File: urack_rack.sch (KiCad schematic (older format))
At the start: 20 parts, among them J1 Screw_Terminal_01x03, U1 LM1117-5.0, U2 MC7905

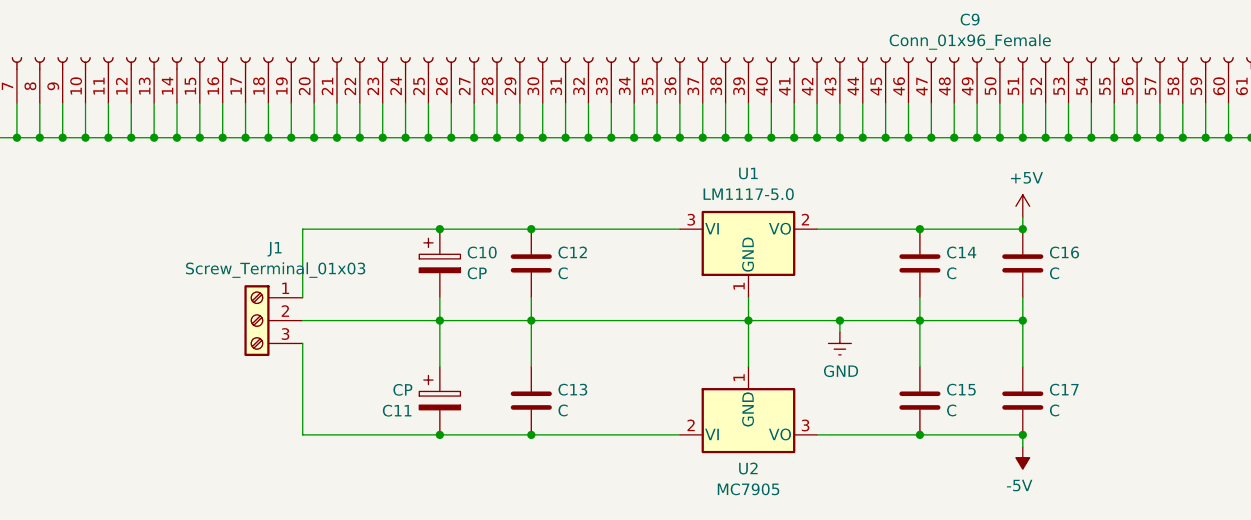
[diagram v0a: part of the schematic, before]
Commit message: Delete LDO. New size connector
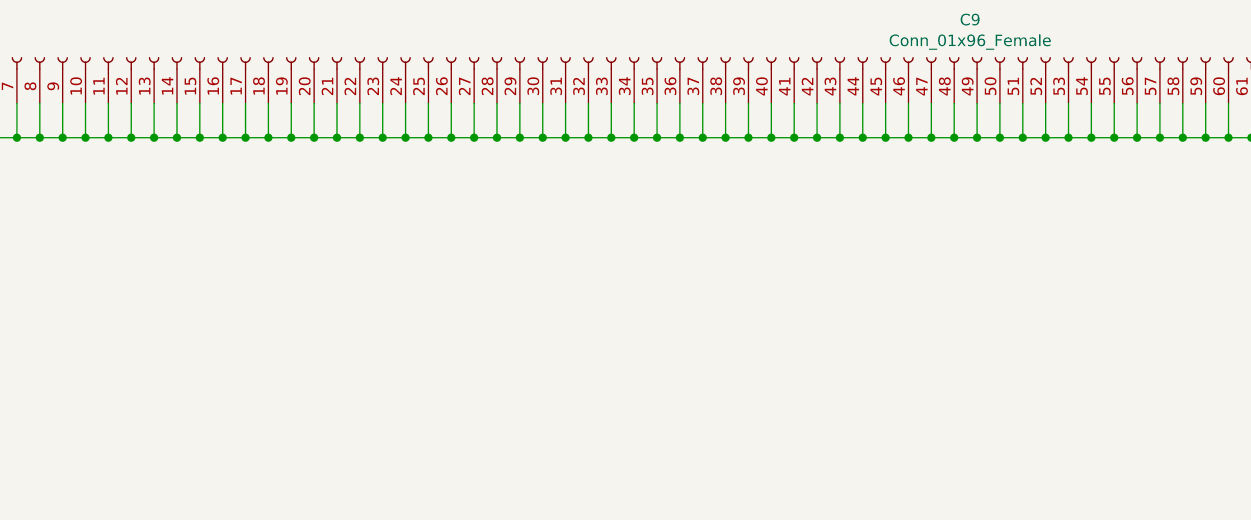
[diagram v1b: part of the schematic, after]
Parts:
- removed C10, C11: CP, Capacitor_SMD:CP_Elec_6.3x7.7, symbol Device:CP
- removed C12, C13, C14, C15, C16, C17: C, Capacitor_SMD:C_0603_1608Metric_Pad1.05x0.95mm_HandSolder, symbol Device:C
- removed J1: Screw_Terminal_01x03, TerminalBlock_Phoenix:TerminalBlock_Phoenix_PT-1,5-3-3.5-H_1x03_P3.50mm_Horizontal, symbol Connector:Screw_Terminal_01x03
- removed U1: LM1117-5.0, Package_TO_SOT_SMD:TO-252-2, symbol Regulator_Linear:LM1117-5.0
- removed U2: MC7905, Package_TO_SOT_SMD:TO-263-3_TabPin2, symbol Regulator_Linear:MC7905
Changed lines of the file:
@@
 Wire Wire Line
 	8050 1800 7950 1800
-$Comp
-L Regulator_Linear:LM1117-5.0 U1
-U 1 1 5FD46628
-P 4550 6450
-F 0 "U1" H 4550 6692 50  0000 C CNN
-F 1 "LM1117-5.0" H 4550 6601 50  0000 C CNN
-F 2 "Package_TO_SOT_SMD:TO-252-2" H 4550 6450 50  0001 C CNN
-F 3 "http://www.ti.com/lit/ds/symlink/lm1117.pdf" H 4550 6450 50  0001 C CNN
-	1    4550 6450
-	1    0    0    -1
-$EndComp
-$Comp
-L Regulator_Linear:MC7905 U2
-U 1 1 5FD495BC
-P 4550 7350
-F 0 "U2" H 4550 7201 50  0000 C CNN
-F 1 "MC7905" H 4550 7110 50  0000 C CNN
-F 2 "Package_TO_SOT_SMD:TO-263-3_TabPin2" H 4550 7150 50  0001 C CIN
-F 3 "http://www.onsemi.com/pub/Collateral/MC7900-D.PDF" H 4550 7350 50  0001 C CNN
-	1    4550 7350
-	1    0    0    -1
-$EndComp
-Wire Wire Line
-	4550 6750 4550 6850
-$Comp
-L uRack:GND #PWR0104
-U 1 1 6073BE97
-P 4950 6900
-F 0 "#PWR0104" H 4950 6650 50  0001 C CNN
-F 1 "GND" H 4955 6727 50  0000 C CNN
-F 2 "" H 4950 6900 50  0001 C CNN
-F 3 "" H 4950 6900 50  0001 C CNN
-	1    4950 6900
-	1    0    0    -1
-$EndComp
-$Comp
-L uRack:+5V #PWR0105
-U 1 1 6073C5B9
-P 5750 6400
-F 0 "#PWR0105" H 5750 6250 50  0001 C CNN
-F 1 "+5V" H 5765 6573 50  0000 C CNN
-F 2 "" H 5750 6400 50  0001 C CNN
-F 3 "" H 5750 6400 50  0001 C CNN
-	1    5750 6400
-	1    0    0    -1
-$EndComp
-$Comp
-L uRack:-5V #PWR0106
-U 1 1 6073FBF9
-P 5750 7400
-F 0 "#PWR0106" H 5750 7500 50  0001 C CNN
-F 1 "-5V" H 5765 7573 50  0000 C CNN
-F 2 "" H 5750 7400 50  0001 C CNN
-F 3 "" H 5750 7400 50  0001 C CNN
-	1    5750 7400
-	-1   0    0    1
-$EndComp
-Wire Wire Line
-	4850 7350 5300 7350
-Wire Wire Line
-	5750 7350 5750 7400
-Wire Wire Line
-	4850 6450 5300 6450
-Wire Wire Line
-	5750 6450 5750 6400
-Wire Wire Line
-	4550 6850 4950 6850
-Wire Wire Line
-	4950 6850 4950 6900
-Connection ~ 4550 6850
-Wire Wire Line
-	4550 6850 4550 7050
-$Comp
-L Device:C C12
-U 1 1 6114C496
-P 3600 6600
-F 0 "C12" H 3715 6646 50  0000 L CNN
-F 1 "C" H 3715 6555 50  0000 L CNN
-F 2 "Capacitor_SMD:C_0603_1608Metric_Pad1.05x0.95mm_HandSolder" H 3638 6450 50  0001 C CNN
-F 3 "~" H 3600 6600 50  0001 C CNN
-	1    3600 6600
-	1    0    0    -1
-$EndComp
-$Comp
-L Device:C C13
-U 1 1 6114E359
-P 3600 7200
-F 0 "C13" H 3715 7246 50  0000 L CNN
-F 1 "C" H 3715 7155 50  0000 L CNN
-F 2 "Capacitor_SMD:C_0603_1608Metric_Pad1.05x0.95mm_HandSolder" H 3638 7050 50  0001 C CNN
-F 3 "~" H 3600 7200 50  0001 C CNN
-	1    3600 7200
-	1    0    0    -1
-$EndComp
-$Comp
-L Device:C C14
-U 1 1 6114F64B
-P 5300 6600
-F 0 "C14" H 5415 6646 50  0000 L CNN
-F 1 "C" H 5415 6555 50  0000 L CNN
-F 2 "Capacitor_SMD:C_0603_1608Metric_Pad1.05x0.95mm_HandSolder" H 5338 6450 50  0001 C CNN
-F 3 "~" H 5300 6600 50  0001 C CNN
-	1    5300 6600
-	1    0    0    -1
-$EndComp
-Connection ~ 5300 6450
-Wire Wire Line
-	5300 6450 5750 6450
-$Comp
-L Device:C C15
-U 1 1 611520D9
-P 5300 7200
-F 0 "C15" H 5415 7246 50  0000 L CNN
-F 1 "C" H 5415 7155 50  0000 L CNN
-F 2 "Capacitor_SMD:C_0603_1608Metric_Pad1.05x0.95mm_HandSolder" H 5338 7050 50  0001 C CNN
-F 3 "~" H 5300 7200 50  0001 C CNN
-	1    5300 7200
-	1    0    0    -1
-$EndComp
-Connection ~ 5300 7350
-Wire Wire Line
-	5300 7350 5750 7350
-$Comp
-L Device:C C16
-U 1 1 61152873
-P 5750 6600
-F 0 "C16" H 5865 6646 50  0000 L CNN
-F 1 "C" H 5865 6555 50  0000 L CNN
-F 2 "Capacitor_SMD:C_0603_1608Metric_Pad1.05x0.95mm_HandSolder" H 5788 6450 50  0001 C CNN
-F 3 "~" H 5750 6600 50  0001 C CNN
-	1    5750 6600
-	1    0    0    -1
-$EndComp
-Connection ~ 5750 6450
-$Comp
-L Device:C C17
-U 1 1 61153349
-P 5750 7200
-F 0 "C17" H 5865 7246 50  0000 L CNN
-F 1 "C" H 5865 7155 50  0000 L CNN
-F 2 "Capacitor_SMD:C_0603_1608Metric_Pad1.05x0.95mm_HandSolder" H 5788 7050 50  0001 C CNN
-F 3 "~" H 5750 7200 50  0001 C CNN
-	1    5750 7200
-	1    0    0    -1
-$EndComp
-Connection ~ 5750 7350
-$Comp
-L Device:CP C10
-U 1 1 61153D94
-P 3200 6600
-F 0 "C10" H 3318 6646 50  0000 L CNN
-F 1 "CP" H 3318 6555 50  0000 L CNN
-F 2 "Capacitor_SMD:CP_Elec_6.3x7.7" H 3238 6450 50  0001 C CNN
-F 3 "~" H 3200 6600 50  0001 C CNN
-	1    3200 6600
-	1    0    0    -1
-$EndComp
-$Comp
-L Device:CP C11
-U 1 1 611547D1
-P 3200 7200
-F 0 "C11" H 3082 7154 50  0000 R CNN
-F 1 "CP" H 3082 7245 50  0000 R CNN
-F 2 "Capacitor_SMD:CP_Elec_6.3x7.7" H 3238 7050 50  0001 C CNN
-F 3 "~" H 3200 7200 50  0001 C CNN
-	1    3200 7200
-	1    0    0    -1
-$EndComp
-$Comp
-L Connector:Screw_Terminal_01x03 J1
-U 1 1 6115501D
-P 2400 6850
-F 0 "J1" H 2318 7167 50  0000 C CNN
-F 1 "Screw_Terminal_01x03" H 2318 7076 50  0000 C CNN
-F 2 "TerminalBlock_Phoenix:TerminalBlock_Phoenix_PT-1,5-3-3.5-H_1x03_P3.50mm_Horizontal" H 2400 6850 50  0001 C CNN
-F 3 "~" H 2400 6850 50  0001 C CNN
-	1    2400 6850
-	-1   0    0    -1
-$EndComp
-Wire Wire Line
-	3200 6450 3600 6450
-Connection ~ 3200 6450
-Connection ~ 3600 6450
-Wire Wire Line
-	4550 6850 3600 6850
-Wire Wire Line
-	2600 6750 2600 6450
-Wire Wire Line
-	2600 6450 3200 6450
-Wire Wire Line
-	2600 6950 2600 7350
-Connection ~ 3600 7350
-Wire Wire Line
-	3200 6750 3200 6850
-Connection ~ 3200 6850
-Wire Wire Line
-	3200 6850 2600 6850
-Wire Wire Line
-	3200 7050 3200 6850
-Wire Wire Line
-	3600 7050 3600 6850
-Connection ~ 3600 6850
-Wire Wire Line
-	3600 6850 3200 6850
-Wire Wire Line
-	3600 6750 3600 6850
-Wire Wire Line
-	4950 6850 5300 6850
-Wire Wire Line
-	5750 6850 5750 6750
-Connection ~ 4950 6850
-Wire Wire Line
-	5750 6850 5750 7050
-Connection ~ 5750 6850
-Wire Wire Line
-	5300 7050 5300 6850
-Connection ~ 5300 6850
-Wire Wire Line
-	5300 6850 5750 6850
-Wire Wire Line
-	5300 6750 5300 6850
-Wire Wire Line
-	2600 7350 3200 7350
-Connection ~ 3200 7350
-Wire Wire Line
-	3200 7350 3600 7350
-Wire Wire Line
-	3600 6450 4250 6450
-Wire Wire Line
-	3600 7350 4250 7350
 $EndSCHEMATC
